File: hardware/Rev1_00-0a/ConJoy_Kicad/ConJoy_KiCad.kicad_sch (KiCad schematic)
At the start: 21 parts, among them J1 SFV5R-2STBE1HLF, J11 5051102291, J8 0532610271, J9 0532610271, X1 CMS-241535-078L65

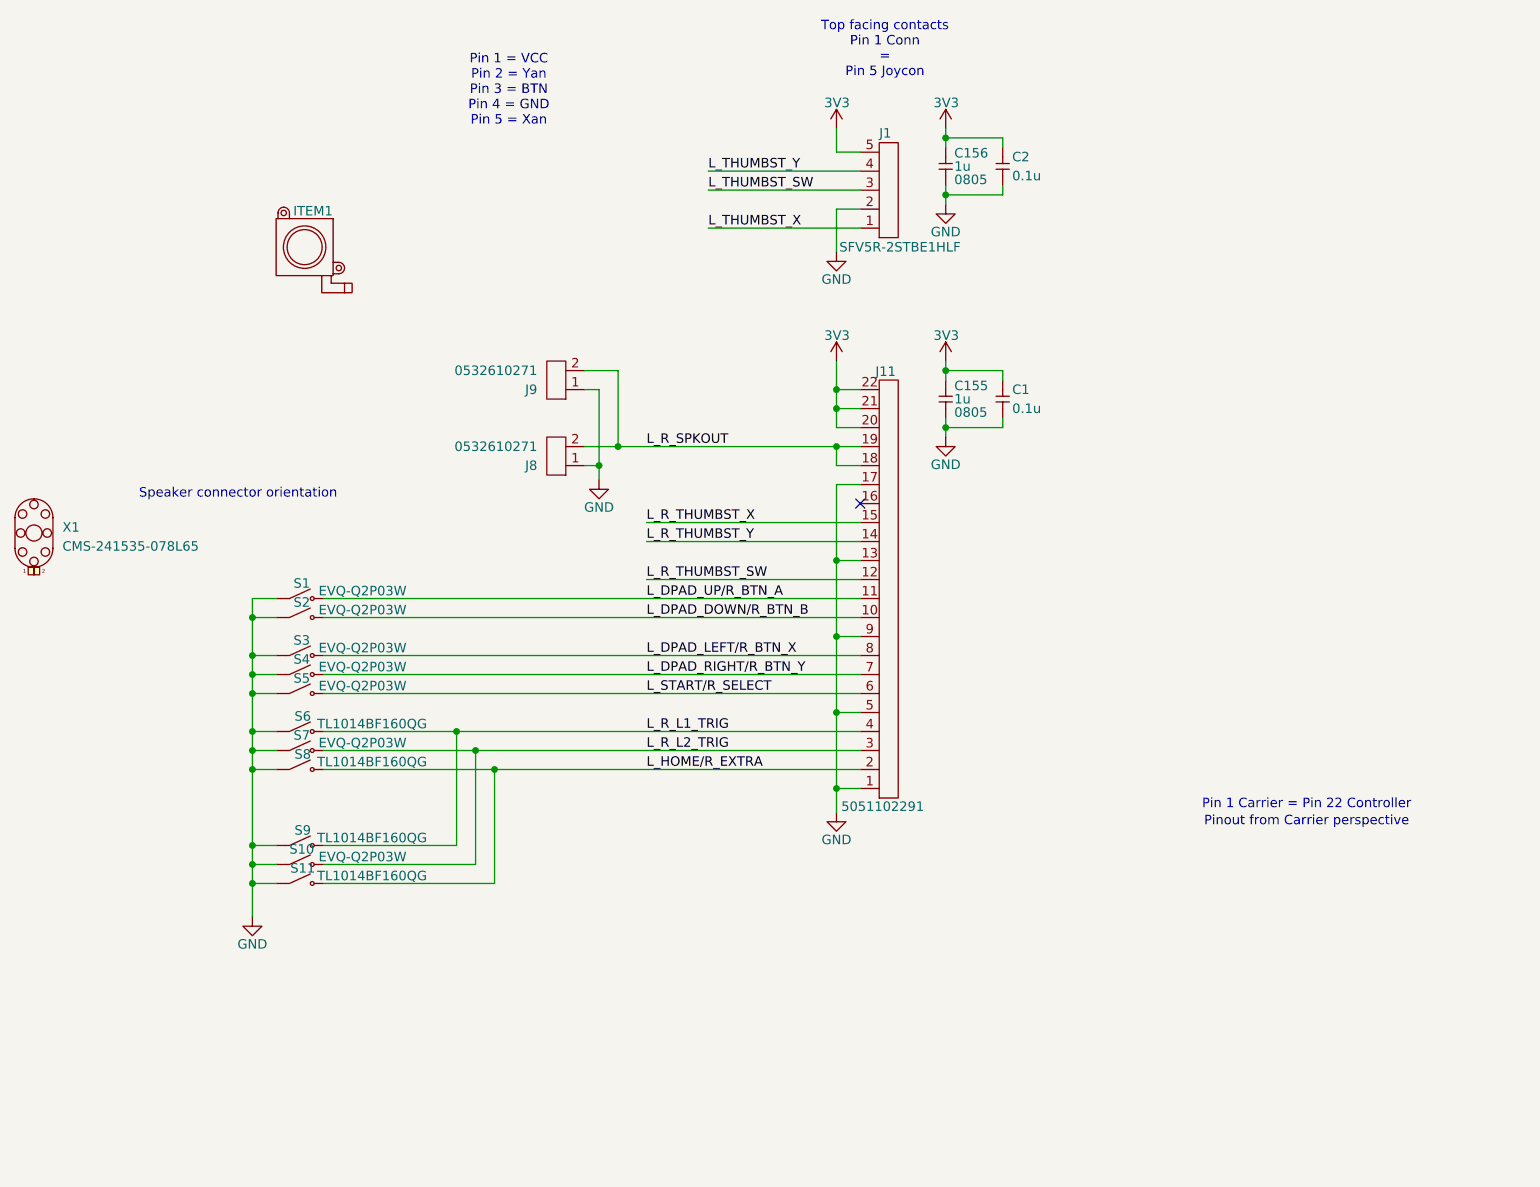
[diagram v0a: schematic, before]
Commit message: Switch speaker pinout following footprint and 3d model review Add mounting holes
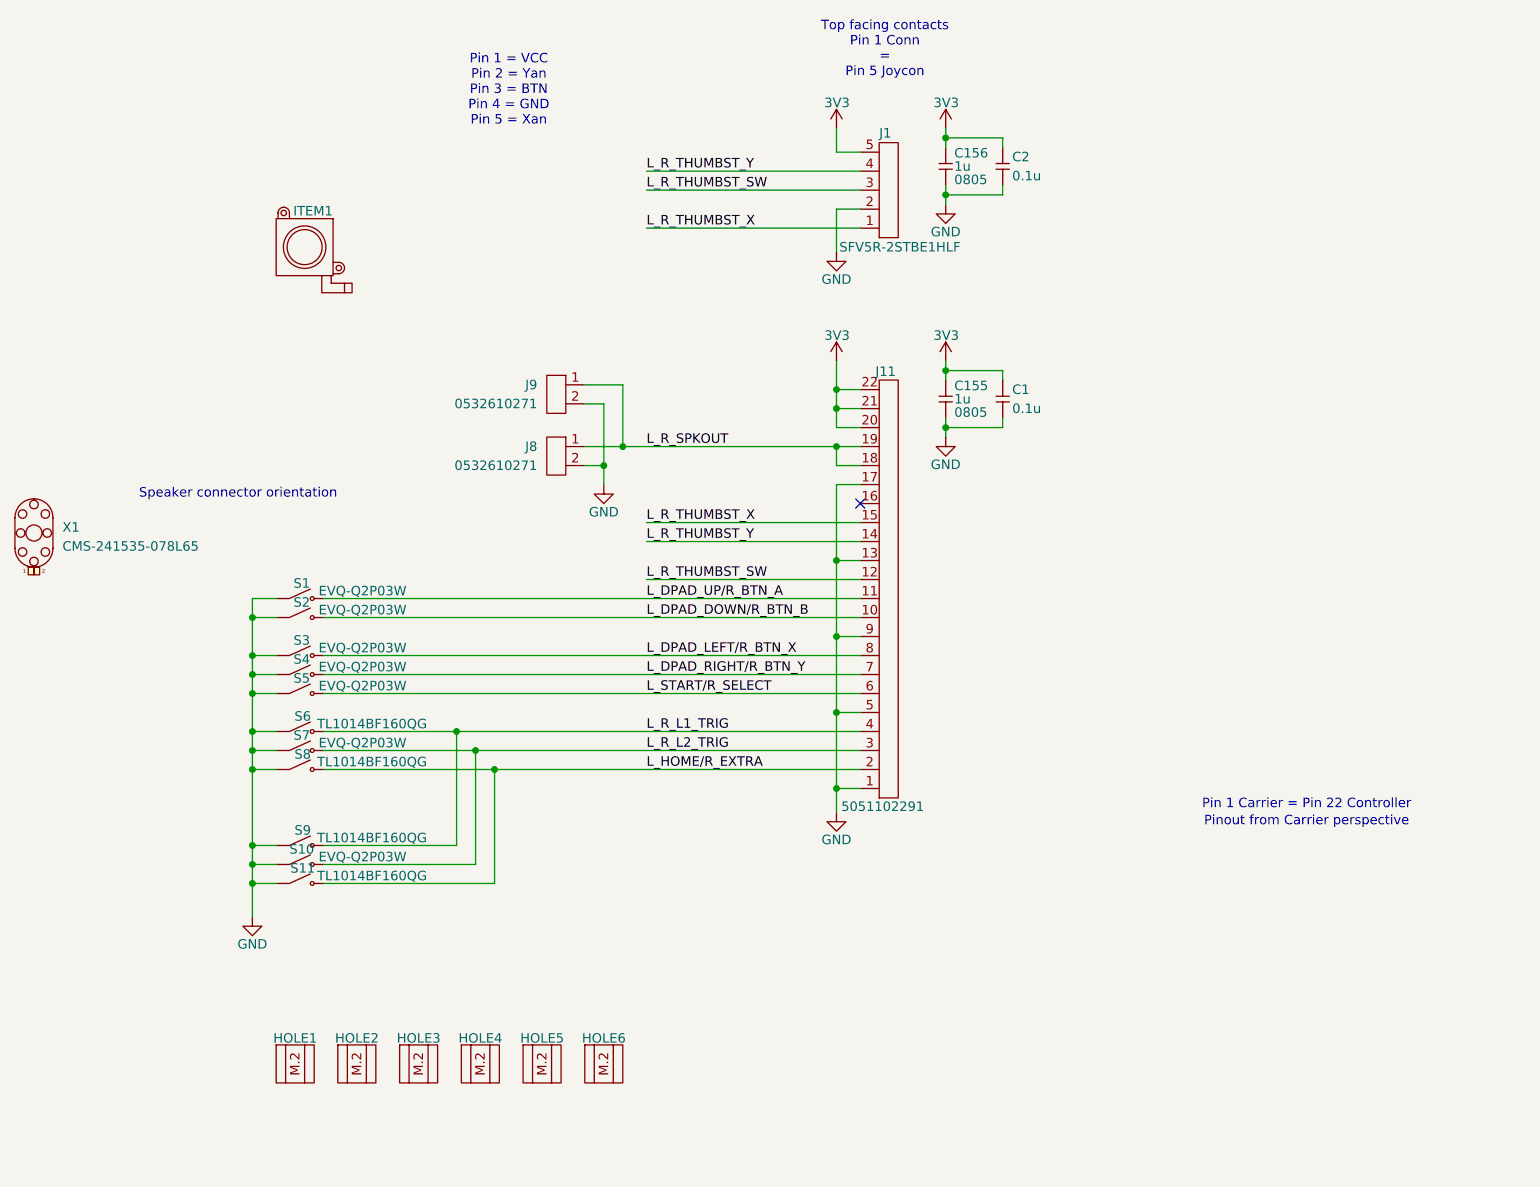
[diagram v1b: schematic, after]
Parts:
- added HOLE1, HOLE2, HOLE3, HOLE4, HOLE5, HOLE6: (no value), footprint:NPTH_M2, symbol KiCad_Lib_Symbols:NPTH_M2
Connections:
- net L_THUMBST_SW is gone; now on net L_R_THUMBST_SW: J1.3
- net L_THUMBST_X is gone; now on net L_R_THUMBST_X: J1.1
- net L_THUMBST_Y is gone; now on net L_R_THUMBST_Y: J1.4
- net GND: now also J8.2, J9.2; no longer J8.1, J9.1
- net L_R_SPKOUT: now also J8.1, J9.1; no longer J8.2, J9.2
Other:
- moved on the sheet: J8, J9

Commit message: ConJoy mostly ready for alpha prototype. Confirm few other potential tweaks at 3d printing
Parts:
- renumbered C156 to C1, C155 to C2, C2 to C3, C1 to C4, J9 to J1, J8 to J2, J1 to J3, J11 to J4
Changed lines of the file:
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@@
 		(in_pos_files yes)
 		(dnp no)
-		(property "Reference" "C155"
+		(property "Reference" "C2"
 			(at 186.563 83.947 90)
 			(show_name no)
@@
 			(project "ConJoy_KiCad"
 				(path "/6e11427c-7ebb-4670-a9a1-99a8ba00a979"
-					(reference "C155")
+					(reference "C2")
 					(unit 1)
 					(variant
@@
 		(in_pos_files yes)
 		(dnp no)
-		(property "Reference" "#PWR0260"
+		(property "Reference" "#PWR010"
 			(at 185.42 97.155 0)
 			(hide yes)
@@
 			(project "ConJoy_KiCad"
 				(path "/6e11427c-7ebb-4670-a9a1-99a8ba00a979"
-					(reference "#PWR0260")
+					(reference "#PWR010")
 					(unit 1)
 					(variant
@@
 		(in_pos_files yes)
 		(dnp no)
-		(property "Reference" "#PWR0259"
+		(property "Reference" "#PWR09"
 			(at 185.42 84.455 0)
 			(hide yes)
@@
 			(project "ConJoy_KiCad"
 				(path "/6e11427c-7ebb-4670-a9a1-99a8ba00a979"
-					(reference "#PWR0259")
+					(reference "#PWR09")
 					(unit 1)
 					(variant
@@
 		(in_bom yes)
 		(on_board yes)
-		(in_pos_files yes)
+		(in_pos_files no)
 		(dnp no)
 		(property "Reference" "S11"
@@
 						(name "Left Controller")
 						(dnp yes)
+						(in_pos_files yes)
 					)
 					(variant
 						(name "Right Controller")
+						(in_pos_files yes)
 					)
 				)
@@
 		(in_bom yes)
 		(on_board yes)
-		(in_pos_files yes)
+		(in_pos_files no)
 		(dnp no)
 		(property "Reference" "S10"
@@
 						(name "Left Controller")
 						(dnp yes)
+						(in_pos_files yes)
 					)
 					(variant
 						(name "Right Controller")
+						(in_pos_files yes)
 					)
 				)
@@
 		(in_pos_files yes)
 		(dnp no)
-		(property "Reference" "#PWR0250"
+		(property "Reference" "#PWR02"
 			(at 139.7 103.505 0)
 			(hide yes)
@@
 			(project "ConJoy_KiCad"
 				(path "/6e11427c-7ebb-4670-a9a1-99a8ba00a979"
-					(reference "#PWR0250")
+					(reference "#PWR02")
 					(unit 1)
 					(variant
@@
 		(in_pos_files yes)
 		(dnp no)
-		(property "Reference" "#PWR0261"
+		(property "Reference" "#PWR03"
 			(at 170.815 53.34 0)
 			(hide yes)
@@
 			(project "ConJoy_KiCad"
 				(path "/6e11427c-7ebb-4670-a9a1-99a8ba00a979"
-					(reference "#PWR0261")
+					(reference "#PWR03")
 					(unit 1)
 					(variant
@@
 		(in_pos_files yes)
 		(dnp no)
-		(property "Reference" "#PWR0262"
+		(property "Reference" "#PWR04"
 			(at 170.815 72.39 0)
 			(hide yes)
@@
 			(project "ConJoy_KiCad"
 				(path "/6e11427c-7ebb-4670-a9a1-99a8ba00a979"
-					(reference "#PWR0262")
+					(reference "#PWR04")
 					(unit 1)
 					(variant
@@
 		(in_pos_files yes)
 		(dnp no)
-		(property "Reference" "#PWR0264"
+		(property "Reference" "#PWR08"
 			(at 185.42 66.04 0)
 			(hide yes)
@@
 			(project "ConJoy_KiCad"
 				(path "/6e11427c-7ebb-4670-a9a1-99a8ba00a979"
-					(reference "#PWR0264")
+					(reference "#PWR08")
 					(unit 1)
 					(variant
@@
 		(in_pos_files yes)
 		(dnp no)
-		(property "Reference" "J1"
+		(property "Reference" "J3"
 			(at 176.53 50.165 0)
 			(show_name no)
@@
 			(project "ConJoy_KiCad"
 				(path "/6e11427c-7ebb-4670-a9a1-99a8ba00a979"
-					(reference "J1")
+					(reference "J3")
 					(unit 1)
 					(variant
@@
 		(in_pos_files yes)
 		(dnp no)
-		(property "Reference" "#PWR0252"
+		(property "Reference" "#PWR01"
 			(at 92.71 161.29 0)
 			(hide yes)
@@
 			(project "ConJoy_KiCad"
 				(path "/6e11427c-7ebb-4670-a9a1-99a8ba00a979"
-					(reference "#PWR0252")
+					(reference "#PWR01")
 					(unit 1)
 					(variant
@@
 		(in_bom yes)
 		(on_board yes)
-		(in_pos_files yes)
+		(in_pos_files no)
 		(dnp no)
 		(property "Reference" "S6"
@@
 						(name "Right Controller")
 						(dnp yes)
+						(in_pos_files yes)
 					)
 				)
@@
 		(in_pos_files yes)
 		(dnp no)
-		(property "Reference" "C2"
+		(property "Reference" "C3"
 			(at 194.31 53.34 90)
 			(show_name no)
@@
 			(project "ConJoy_KiCad"
 				(path "/6e11427c-7ebb-4670-a9a1-99a8ba00a979"
-					(reference "C2")
+					(reference "C3")
 					(unit 1)
 					(variant
@@
 		(in_bom yes)
 		(on_board yes)
-		(in_pos_files yes)
+		(in_pos_files no)
 		(dnp no)
-		(property "Reference" "J9"
+		(property "Reference" "J1"
 			(at 130.81 83.8199 0)
 			(show_name no)
@@
 			(project "ConJoy_KiCad"
 				(path "/6e11427c-7ebb-4670-a9a1-99a8ba00a979"
-					(reference "J9")
+					(reference "J1")
 					(unit 1)
 					(variant
 						(name "Left Controller")
 						(dnp yes)
+						(in_pos_files yes)
 					)
 					(variant
 						(name "Right Controller")
+						(in_pos_files yes)
 					)
 				)
@@
 		(in_bom yes)
 		(on_board yes)
-		(in_pos_files yes)
+		(in_pos_files no)
 		(dnp no)
 		(property "Reference" "S8"
@@
 						(name "Right Controller")
 						(dnp yes)
+						(in_pos_files yes)
 					)
 				)
@@
 		(in_bom yes)
 		(on_board yes)
-		(in_pos_files yes)
+		(in_pos_files no)
 		(dnp no)
 		(property "Reference" "S9"
@@
 						(name "Left Controller")
 						(dnp yes)
+						(in_pos_files yes)
 					)
 					(variant
 						(name "Right Controller")
+						(in_pos_files yes)
 					)
 				)
@@
 		(in_pos_files yes)
 		(dnp no)
-		(property "Reference" "C156"
+		(property "Reference" "C1"
 			(at 186.563 52.832 90)
 			(show_name no)
@@
 			(project "ConJoy_KiCad"
 				(path "/6e11427c-7ebb-4670-a9a1-99a8ba00a979"
-					(reference "C156")
+					(reference "C1")
 					(unit 1)
 					(variant
@@
 		(in_pos_files yes)
 		(dnp no)
-		(property "Reference" "J11"
+		(property "Reference" "J4"
 			(at 176.022 82.042 0)
 			(show_name no)
@@
 			(project "ConJoy_KiCad"
 				(path "/6e11427c-7ebb-4670-a9a1-99a8ba00a979"
-					(reference "J11")
+					(reference "J4")
 					(unit 1)
 					(variant
@@
 		(in_pos_files yes)
 		(dnp no)
-		(property "Reference" "#PWR0246"
+		(property "Reference" "#PWR05"
 			(at 170.815 84.455 0)
 			(hide yes)
@@
 			(project "ConJoy_KiCad"
 				(path "/6e11427c-7ebb-4670-a9a1-99a8ba00a979"
-					(reference "#PWR0246")
+					(reference "#PWR05")
 					(unit 1)
 					(variant
@@
 		(in_pos_files yes)
 		(dnp no)
-		(property "Reference" "#PWR0263"
+		(property "Reference" "#PWR07"
 			(at 185.42 53.34 0)
 			(hide yes)
@@
 			(project "ConJoy_KiCad"
 				(path "/6e11427c-7ebb-4670-a9a1-99a8ba00a979"
-					(reference "#PWR0263")
+					(reference "#PWR07")
 					(unit 1)
 					(variant
@@
 		(in_bom yes)
 		(on_board yes)
-		(in_pos_files yes)
+		(in_pos_files no)
 		(dnp no)
 		(property "Reference" "S7"
@@
 						(name "Right Controller")
 						(dnp yes)
+						(in_pos_files yes)
 					)
 				)
@@
 		(in_bom yes)
 		(on_board yes)
-		(in_pos_files yes)
+		(in_pos_files no)
 		(dnp no)
-		(property "Reference" "J8"
+		(property "Reference" "J2"
 			(at 130.81 92.0749 0)
 			(show_name no)
@@
 			(project "ConJoy_KiCad"
 				(path "/6e11427c-7ebb-4670-a9a1-99a8ba00a979"
-					(reference "J8")
+					(reference "J2")
 					(unit 1)
 					(variant
 						(name "Right Controller")
 						(dnp yes)
+						(in_pos_files yes)
 					)
 				)
@@
 		(in_pos_files yes)
 		(dnp no)
-		(property "Reference" "C1"
+		(property "Reference" "C4"
 			(at 194.31 84.455 90)
 			(show_name no)
@@
 			(project "ConJoy_KiCad"
 				(path "/6e11427c-7ebb-4670-a9a1-99a8ba00a979"
-					(reference "C1")
+					(reference "C4")
 					(unit 1)
 					(variant
@@
 		(in_pos_files yes)
 		(dnp no)
-		(property "Reference" "#PWR0248"
+		(property "Reference" "#PWR06"
 			(at 170.815 147.32 0)
 			(hide yes)
@@
 			(project "ConJoy_KiCad"
 				(path "/6e11427c-7ebb-4670-a9a1-99a8ba00a979"
-					(reference "#PWR0248")
+					(reference "#PWR06")
 					(unit 1)
 					(variant

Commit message: Commit ConJoy design + output files (ready for manufacturing or REV 1.00-0A)
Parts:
- added D1: MMSZ5226B-7-F, footprint:SOD-123, symbol KicadCompDb:Diodes/DIODE_00001
- added FID1, FID2, FID3, FID4, FID5, FID6: (no value), footprint:FIDUCIAL, symbol KiCad_Lib_Symbols:FIDUCIAL
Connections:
- net 3V3: now also D1.1 (K)
- net GND: now also D1.2 (A)

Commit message: Add a lillllllll more clearance on inner cutout of ConJoy for Flat Flex cable of joystick
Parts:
- removed ITEM1: HallPi PCB FP, footprint:JoyCon_HallEffect_TMR, symbol KiCad_Lib_Symbols:HallPi PCB FP
- removed X1: CMS-241535-078L65, symbol KicadCompDb:Miscellaneous/MISC_00014

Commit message: Move Joystick connector to bottom side of PCB Remove duplicate decoupling + bulk capacitors
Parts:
- removed C1: 1u, footprint:CAP_NONPOL_0805, symbol KicadCompDb:Capacitors/CAP_CER_SMT_00002
- removed C3: 0.1u, footprint:CAP_NONPOL_0402, symbol KicadCompDb:Capacitors/CAP_CER_SMT_00001
- removed J3: SFV5R-2STBE1HLF, footprint:SFV5R-2ST, symbol KicadCompDb:Connector/CONN_00028
- added J3: SFV5R-1STE1HLF, footprint:SFV5R-1ST, symbol KicadCompDb:Connector/CONN_00030
- renumbered C2 to C1, C4 to C2
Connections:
- net 3V3: now also J3.1
- net GND: now also J3.4
- net L_R_THUMBST_SW: now also J3.3
- net L_R_THUMBST_X: now also J3.5
- net L_R_THUMBST_Y: now also J3.2
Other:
- note added: "Bottom facing contacts Pin 1 Conn = Pin 1 Joycon"
- note removed: "Top facing contacts Pin 1 Conn = Pin 5 Joycon"

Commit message: Update ConJoy L2 trigger (2-level trigger instead) Update ConJoy all output files accordingly
Work on Consolation preliminary placement
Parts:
- removed S10, S7: EVQ-Q2P03W, footprint:EVQQ2, symbol KicadCompDb:Miscellaneous/MISC_00015
- added C3: 1u, footprint:CAP_NONPOL_0805, symbol KicadCompDb:Capacitors/CAP_CER_SMT_00002
- added S10, S7: TL1014BF160QG, footprint:TL1014B, symbol KicadCompDb:Miscellaneous/MISC_00016
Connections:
- net 3V3: now also C3.2
- net GND: now also C3.1, S10.1, S7.1
- net L_R_L2_TRIG: now also S10.2, S7.2
